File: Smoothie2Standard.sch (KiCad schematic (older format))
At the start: 336 parts, among them J2 ADC4, P1 VFET_IN, P10 5V, P11 BETA, P12 JTAG, P13 3.3V, P14 USB_B, P15 USB_A, P16 MICROSD, P17 GAMMA, P19 T1, P2 VBB_IN, P20 T2, P21 T3, P23 SDIO[F], P24 DELTA, P25 XMIN, P26 YMIN, P27 ZMIN, P28 XMAX, P29 YMAX, P3 VFET_IN, P30 ZMAX, P31 PROBE, P39 SSR1, P4 VBB_IN, P40 HOTEND1, P41 FAN, P42 BED1, P43 SSR2, P44 HOTEND2, P45 DAC, P46 RPI, P5 3.3VA, P6 ALPHA, P7 VFET, P8 5VIN, P9 VBB, Q1 PSMN7R0-60YS, Q10 BSS138, Q11 BSS138, Q12 BSS138, Q2 PSMN7R0-60YS, Q3 PMV48XP,215, Q4 BUK9Y43-60E, Q5 BUK9Y43-60E, Q6 SUD50P04-08-GE3, Q7 PMV48XP,215, Q8 PSMN7R0-60YS, Q9 BUK9Y43-60E, SW1 RESET, U1 LPC43xxFET256, U2 A8498, U3 LM1117S33, U4 AP2511, U5 SPI_FLASH, U6 TC4427A, U8 78L12F, X1 12MHz

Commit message: Todo list changes: - series termination for ethernet - wired the three expansion ports - tied EN pins on drivers to gnd - added diode to 5V regulator supply - removed central via from ethernet PHY
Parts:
- removed R107, R108, R109, R110: 10K, Resistors_SMD:R_0402, symbol R
- added D12: D_Small_ALT, Diode_SMD:D_SOD-323, symbol Device:D_Small_ALT
- added R103, R113, R114, R115, R116, R117: 33R, Resistor_SMD:R_0402_1005Metric, symbol Smoothie2Standard-rescue:R
- C1, C10, C11, C12, C13, C15, C16, C17, C18, C19, C2, C20, C27, C29, C3, C30, C32, C33, C34, C35, C38, C39, C4, C40, C42, C43, C44, C45, C46, C47, C48, C49, C5, C50, C51, C55, C56, C57, C6, C7, C8, C9: symbol C_Small -> Smoothie2Standard-rescue:C_Small
- C14, C21, C24, C26, C31, C36, C37, C41: symbol C -> Smoothie2Standard-rescue:C
- C22, C23, C25, C28: symbol CP1 -> Smoothie2Standard-rescue:CP1
- D1, D2, D53, D57: symbol ZENERsmall -> Smoothie2Standard-rescue:ZENERsmall
- D10, D11, D20, D21, D22, D23, D26, D27, D28, D3, D31, D32, D33, D5, D50, D51, D52, D56, D6, D7, D8, D9: symbol D_Schottky_Small -> Smoothie2Standard-rescue:D_Schottky_Small
- D13, D14, D15, D16, D17, D18, D19, D24, D25, D29, D30, D54, D55: symbol LED-RESCUE-Smoothie2Standard -> Smoothie2Standard-rescue:LED-RESCUE-Smoothie2Standard
- D4: symbol D_Schottky -> Smoothie2Standard-rescue:D_Schottky
- G1, G2, G3, G4, G5, G6, G7, G8, G9, P12, P23, P46: symbol CONN_02X05 -> Smoothie2Standard-rescue:CONN_02X05
- J2: symbol Conn_01x01 -> Smoothie2Standard-rescue:Conn_01x01
- JP1, JP16, JP17, JP5, JP6, JP8: symbol JUMPER3 -> Smoothie2Standard-rescue:JUMPER3
- JP10, JP11, JP12, JP13, JP14, JP15, JP2, JP3, JP4, JP7, JP9: symbol Jumper_NC_Small -> Smoothie2Standard-rescue:Jumper_NC_Small
- L1, L10, L2, L3, L4, L5, L6, L7, L8, L9: symbol INDUCTOR_SMALL -> Smoothie2Standard-rescue:INDUCTOR_SMALL
- P1, P10, P13, P19, P2, P20, P21, P3, P4, P40, P41, P42, P44, P45, P5, P7, P8, P9: symbol CONN_01X02 -> Smoothie2Standard-rescue:CONN_01X02
- P11, P17, P24, P31, P6: symbol CONN_01X04 -> Smoothie2Standard-rescue:CONN_01X04
- P14: symbol USB_B -> Smoothie2Standard-rescue:USB_B
- P15: symbol USB_A -> Smoothie2Standard-rescue:USB_A
- P16: symbol MICROSD -> microsd:MICROSD
- P25, P26, P27, P28, P29, P30, P39, P43: symbol CONN_01X03 -> Smoothie2Standard-rescue:CONN_01X03
- Q1, Q2, Q4, Q5, Q8, Q9: symbol Q_NMOS_SSSGD -> q_nmos_sssgd:Q_NMOS_SSSGD
- Q10, Q11, Q12: symbol BSS138 -> Smoothie2Standard-rescue:BSS138
- Q3, Q7: symbol Q_PMOS_GSD -> Smoothie2Standard-rescue:Q_PMOS_GSD
- Q6: symbol Q_PMOS_GDS -> Smoothie2Standard-rescue:Q_PMOS_GDS
- R1, R10, R101, R102, R104, R105, R106, R11, R111, R112, R12, R13, R14, R15, R16, R17, R18, R19, R2, R20, R21, R22, R23, R24, R25, R26, R27, R28, R29, R3, R30, R31, R32, R33, R34, R35, R36, R37, R38, R39, R4, R40, R41, R42, R43, R44, R45, R46, R47, R48, R49, R5, R50, R51, R52, R53, R54, R55, R56, R57, R58, R59, R6, R60, R61, R62, R63, R64, R65, R66, R67, R68, R69, R7, R70, R71, R72, R73, R74, R75, R76, R77, R78, R79, R8, R80, R81, R9: symbol R -> Smoothie2Standard-rescue:R
- SW1: symbol SW_PUSH_SMALL_H -> Smoothie2Standard-rescue:SW_PUSH_SMALL_H
- U1: symbol LPC43xxFET256 -> lpc43xxfet256:LPC43xxFET256
- U2: symbol A8498 -> a8498:A8498
- U3: symbol LM1117 -> lm1117:LM1117
- U4: symbol AP2511 -> ap2511:AP2511
- U5: symbol SPI_FLASH -> spi_flash:SPI_FLASH
- U6: symbol TC4427A -> tc4427a:TC4427A
- U8: symbol R78E -> r78e:R78E
- W1, W10, W11, W12, W13, W14, W15, W16, W17, W18, W19, W2, W20, W21, W22, W23, W24, W25, W26, W27, W28, W29, W3, W30, W31, W32, W33, W34, W35, W36, W37, W38, W39, W4, W40, W41, W42, W43, W44, W45, W46, W47, W48, W49, W5, W50, W51, W52, W53, W54, W55, W6, W7, W8, W9: symbol TEST_1P -> Smoothie2Standard-rescue:TEST_1P
- X1: symbol CRYSTAL_SMD -> Smoothie2Standard-rescue:CRYSTAL_SMD
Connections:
- wire segments 1206 -> 1455
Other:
- note added: "MAC to PHY signals terminated here\nPHY to MAC signals terminated on PHY end"

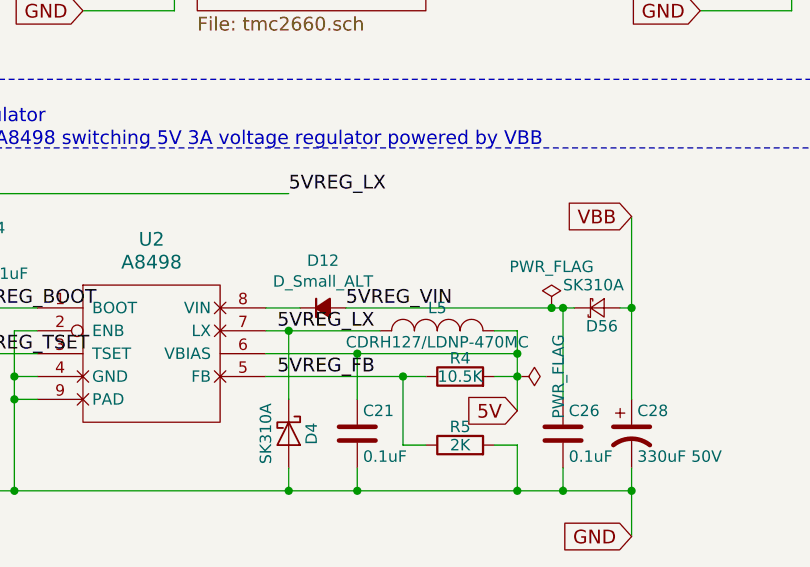
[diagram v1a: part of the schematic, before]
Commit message: remove extra diode on 5vreg_vin
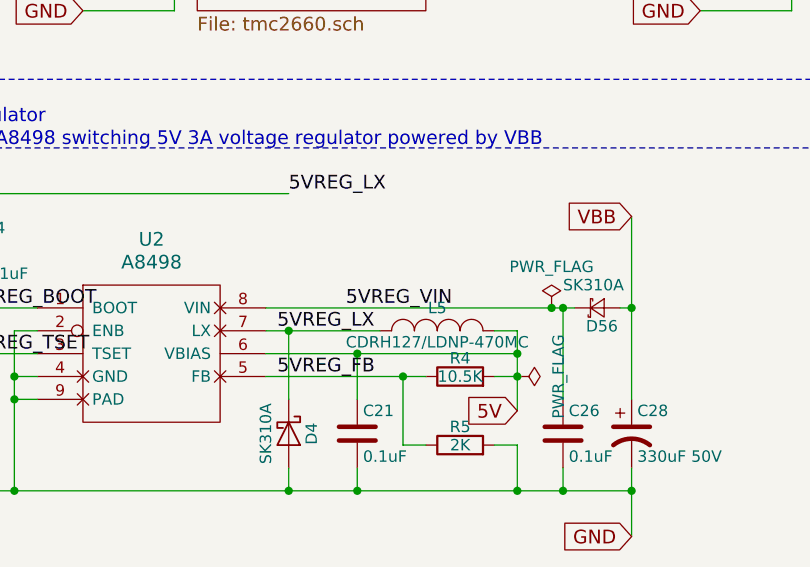
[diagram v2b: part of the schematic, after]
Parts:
- removed D12: D_Small_ALT, Diode_SMD:D_SOD-323, symbol Device:D_Small_ALT
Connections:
- wire segments 1455 -> 1454
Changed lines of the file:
@@
 Wire Wire Line
 	9000 13100 9400 13100
-Wire Wire Line
-	4750 14400 5650 14400
 Connection ~ 5700 14400
-$Comp
-L Device:D_Small_ALT D12
-U 1 1 61659750
-P 4650 14400
-F 0 "D12" H 4650 14607 50  0000 C CNN
-F 1 "D_Small_ALT" H 4650 14516 50  0000 C CNN
-F 2 "Diode_SMD:D_SOD-323" V 4650 14400 50  0001 C CNN
-F 3 "~" V 4650 14400 50  0001 C CNN
-	1    4650 14400
-	1    0    0    -1
-$EndComp
-Wire Wire Line
-	4550 14400 4400 14400
 Text Label 4500 13900 0    60   ~ 0
 5VREG_LX
@@
 Wire Wire Line
 	5650 14400 5700 14400
+Wire Wire Line
+	4400 14400 5650 14400
 $EndSCHEMATC
